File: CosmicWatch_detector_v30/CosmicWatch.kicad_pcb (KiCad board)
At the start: 2 copper layers, 140.8 x 104 mm, 111 parts, among them J3 RJ45, P1 CONN_01X04, P10 CONN_02X02, P11 CONN_01X01, P12 CONN_01X01, P13 CONN_01X01, P14 CONN_01X01, P15 CONN_02X04, P16 CONN_01X02, P19 CONN_01X01, P2 CONN_01X01, P29 CONN_01X01, P3 CONN_01X04, P30 CONN_01X01, P32 CONN_01X04, P4 CONN_01X04, P5 CONN_01X02, P7 CONN_01X01, P8 CONN_01X01, SW1 RESET, U1 LT3461, U10 SiPM_AFBR-S4N33C013, U12 LTC6752, U13 TS5A1066, U16 UMCC, U17 UMCC, U19 LMH6658, U2 SiPM_MicroFJ−300XX−TSV, U22 UMCC, U23 UMCC, U3 MMCX, U4 TS5A1066, U5 RasberryPi_Pico, U6 LMH6658, U7 TPS6040X, U8 sd_card_socket, U9 2NPNMBT6429DW1T1G

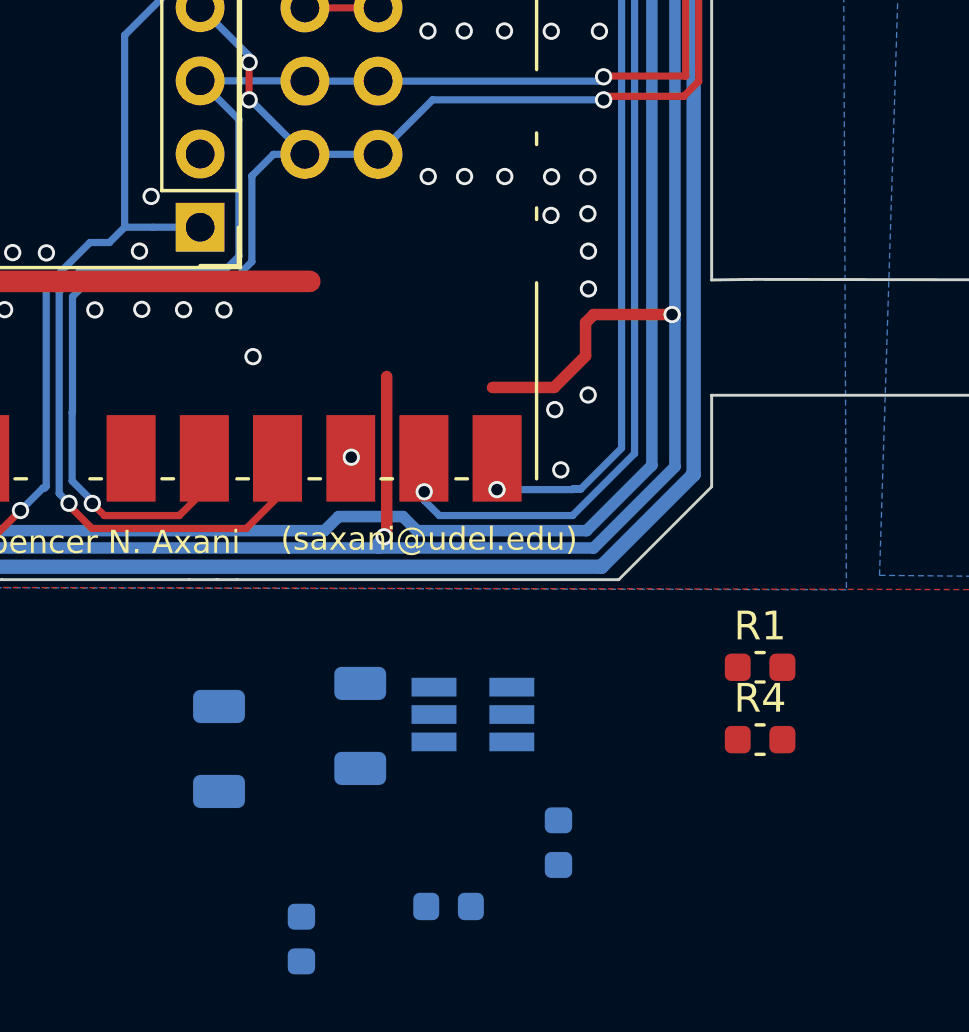
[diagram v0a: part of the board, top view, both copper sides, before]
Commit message: adding DC-DC booster on v3 schematics and pcb
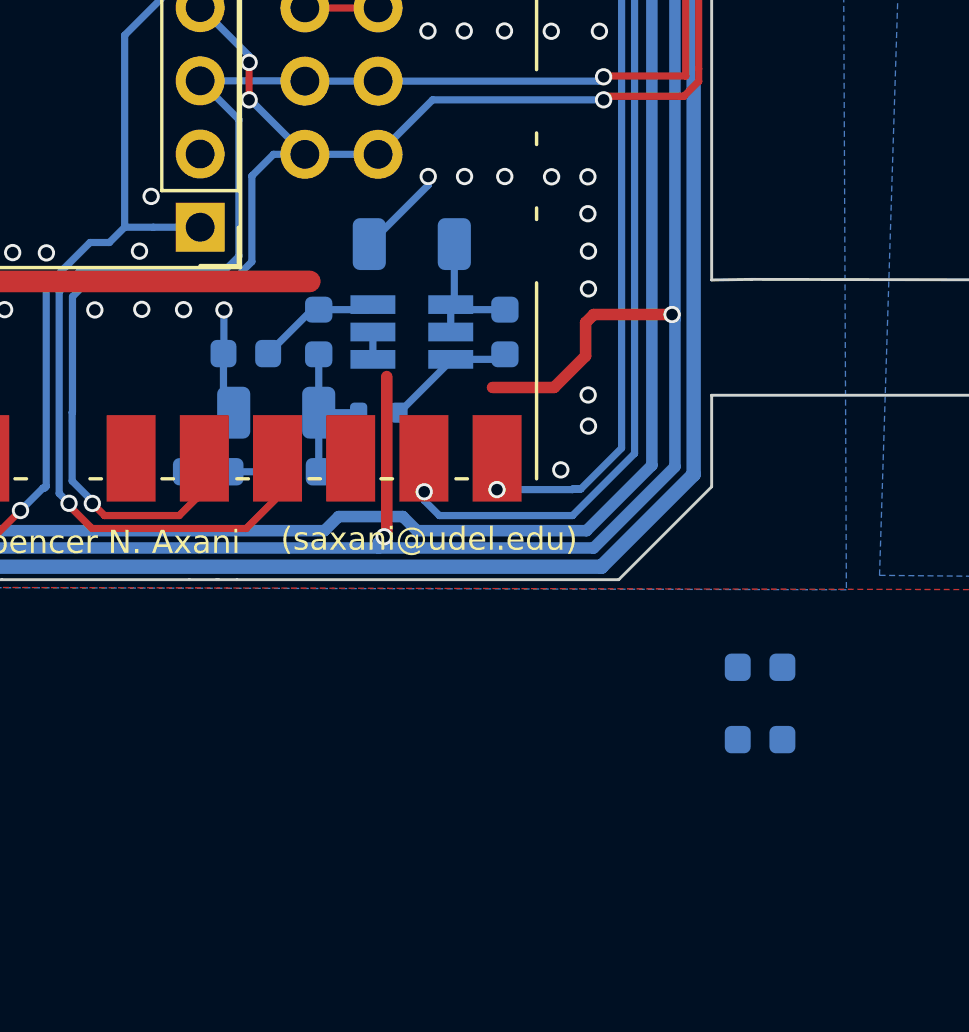
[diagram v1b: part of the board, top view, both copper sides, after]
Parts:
- removed C27: 2.2u, Capacitor_SMD:C_0603_1608Metric
- added C4: 1uF, Capacitor_SMD:C_0603_1608Metric, B.Cu at (179.8, 126.0)
- added D4: D_Schottky, Diode_SMD:D_SOD-523, B.Cu at (185.7, 123.9)
- added R10: 6.65k, Capacitor_SMD:C_0603_1608Metric, B.Cu at (181.1, 121.9)
- added R25: 100, Capacitor_SMD:C_0603_1608Metric, B.Cu at (182.8, 126.0)
- C2: value 4.7u -> 2.2uF
- C3: value 2.2u -> 2.2uF
- R1, R4: moved to B.Cu
- R2: value 1k -> 147k
- R24: value 10k -> 100k
- R40: value 100 -> 100k
- U1: value LT3461 -> MAX5026
- moved R2 21.1 mm to (183.6, 121.1), turned to -90 degrees
- moved L1 17.8 mm to (190.1, 121.1)
- moved C2 16.8 mm to (186.8, 118.1), turned to 180 degrees
- moved U1 13.4 mm to (186.8, 121.1), turned to 0 degrees
- moved C3 11.8 mm to (182.1, 123.9), turned to 180 degrees
- turned R1 to 180 degrees
- turned R4 to 180 degrees
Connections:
- C3 pad 1: HV -> Net-(D4-K)
- L1 pad 1: VCC -> Net-(D4-A)
- L1 pad 2: unconnected-(L1-Pad2) -> VCC
- R2 pad 1: unconnected-(R2-Pad1) -> Net-(U1-FB)
- R2 pad 2: HV -> Net-(D4-K)
- U1 pad 1: unconnected-(U1-sw-Pad1) -> GNDA
- U1 pad 2: unconnected-(U1-gnd-Pad2) -> GNDA
- U1 pad 3: unconnected-(U1-FB-Pad3) -> Net-(U1-FB)
- U1 pad 4: unconnected-(U1-SDWN-Pad4) -> VCC
- U1 pad 5: unconnected-(U1-Vout-Pad5) -> VCC
- U1 pad 6: VCC -> Net-(D4-A)
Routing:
- net GNDA: track 30.1 -> 40.7 mm, vias 319 -> 316
- net VCC: track 219.7 -> 226.3 mm
- net Net-(D4-K): track 0.00 -> 5.46 mm
- net Net-(D4-A): track 0.00 -> 4.55 mm
- net Net-(U1-FB): track 0.00 -> 4.34 mm

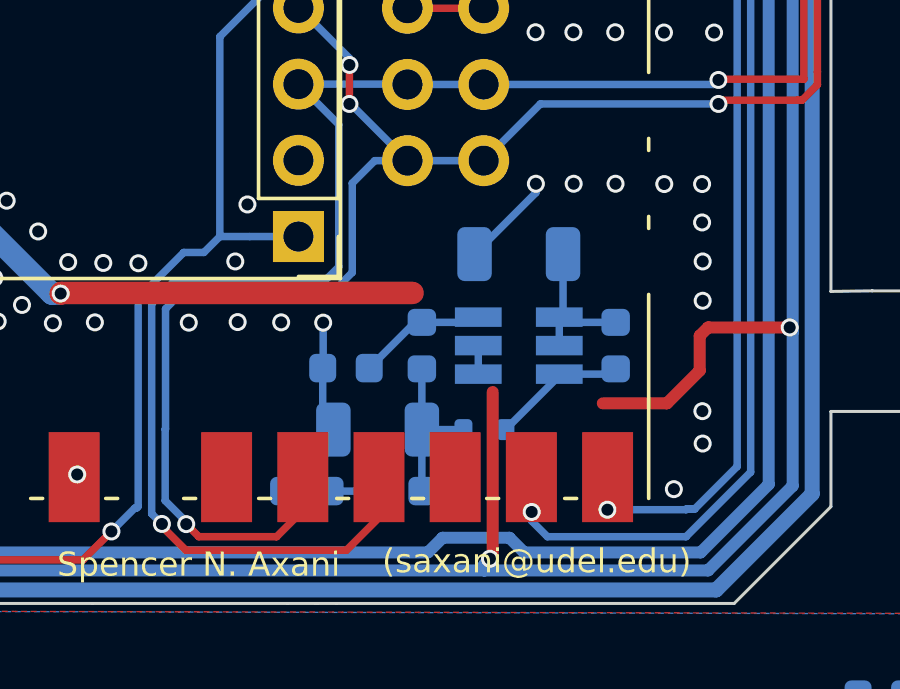
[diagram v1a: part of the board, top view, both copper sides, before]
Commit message: fixing misplaced VCC conection
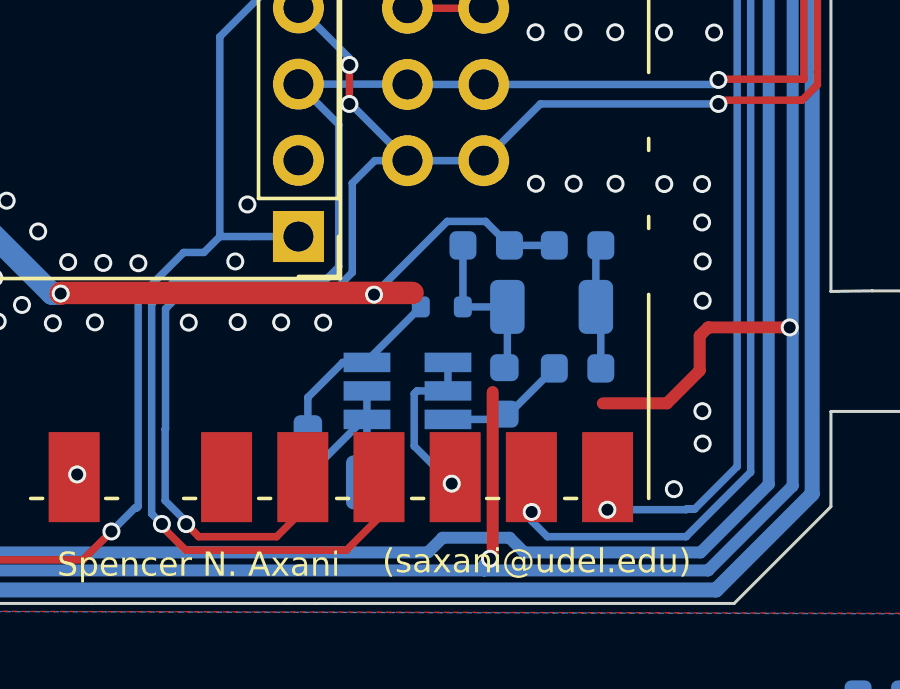
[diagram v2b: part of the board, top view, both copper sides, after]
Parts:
- moved C4 12.2 mm to (188.8, 117.8), turned to 0 degrees
- moved L1 10.9 mm to (179.8, 124.7), turned to -90 degrees
- moved R25 8.69 mm to (185.8, 117.8), turned to 180 degrees
- moved C2 8.47 mm to (183.1, 125.7), turned to 0 degrees
- moved R10 7.72 mm to (188.8, 121.9), turned to 180 degrees
- moved C3 7.10 mm to (187.9, 119.8), turned to 0 degrees
- moved D4 4.33 mm to (184.3, 119.8), turned to 180 degrees
- moved U1 4.01 mm to (183.1, 122.6), turned to 180 degrees
- moved R2 3.14 mm to (186.4, 122.6), turned to 90 degrees
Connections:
- C4 pad 1: VCC -> HV
- R25 pad 1: VCC -> HV
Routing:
- net HV: track 34.2 -> 41.5 mm, vias 3 -> 4
- net Net-(D4-A): track 4.55 -> 6.09 mm
- net GNDA: track 40.7 -> 40.0 mm, vias 316 -> 317
- net VCC: track 226.3 -> 225.6 mm

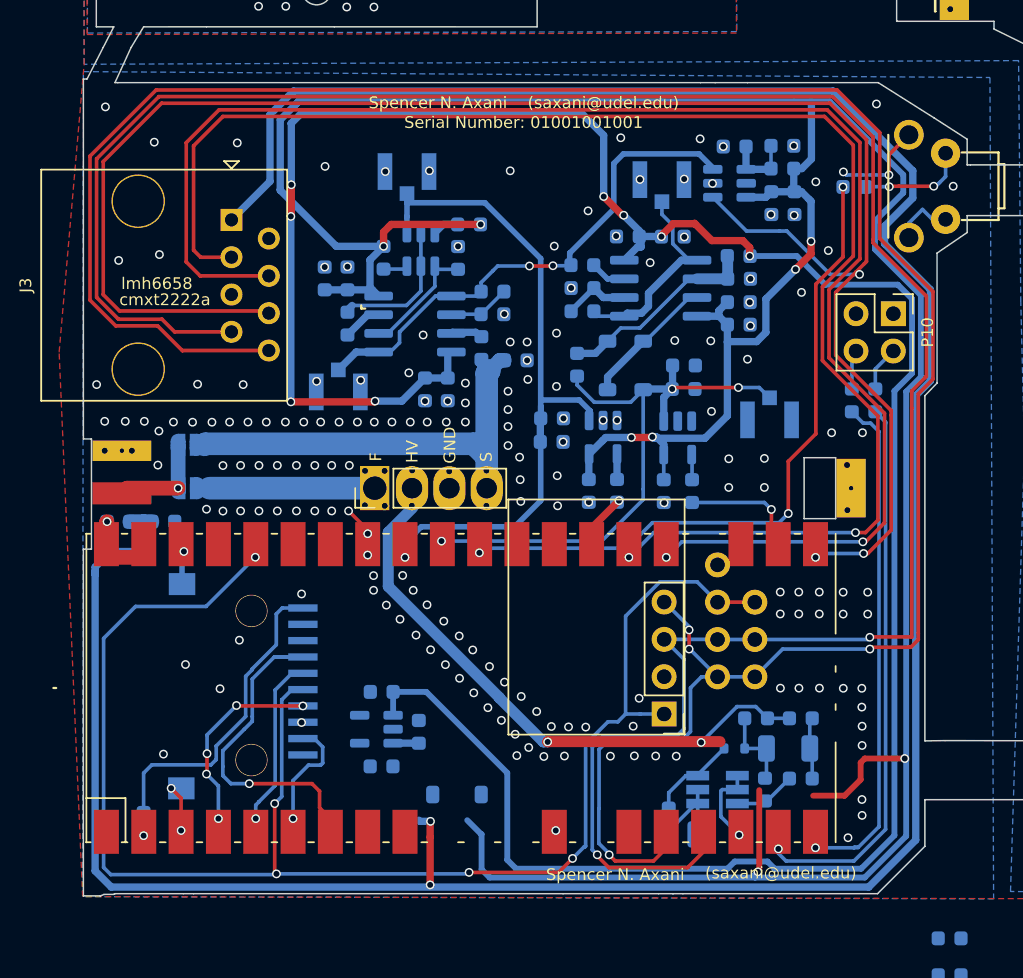
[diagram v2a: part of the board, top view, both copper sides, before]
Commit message: rearranging DC-DC booster components
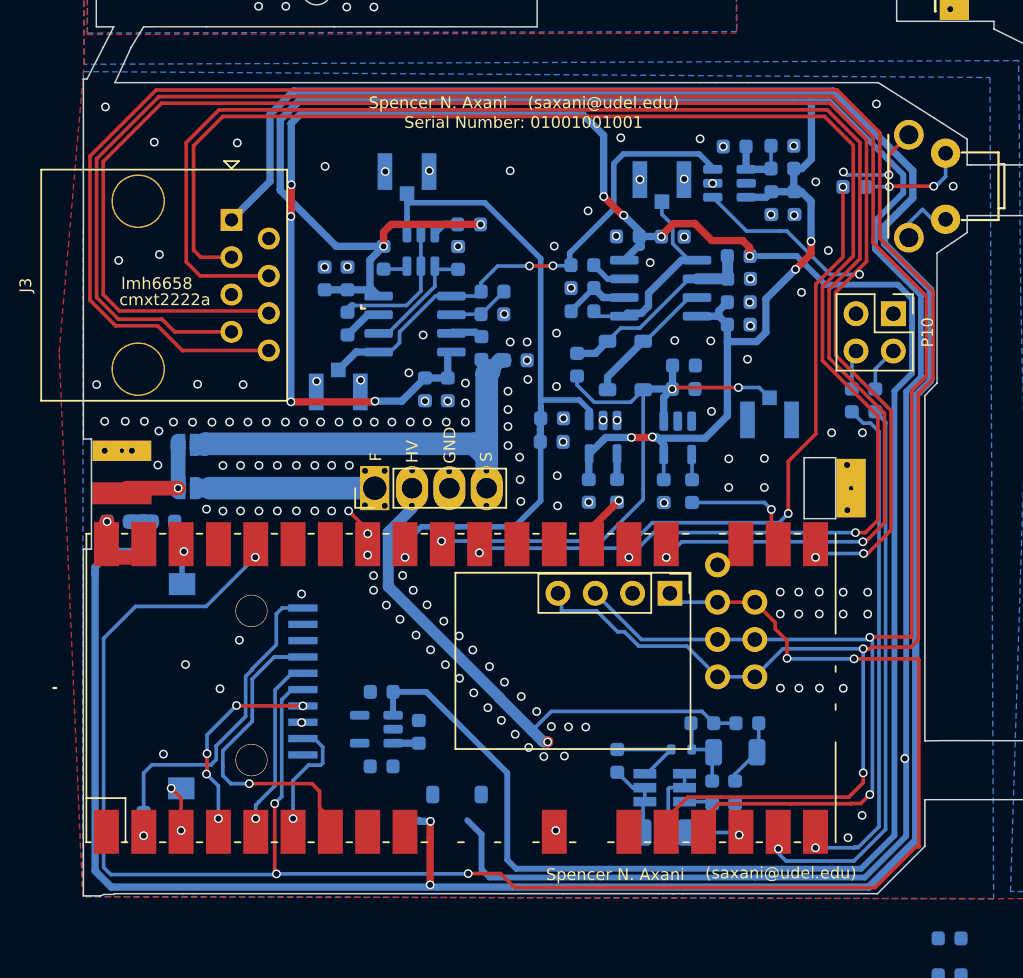
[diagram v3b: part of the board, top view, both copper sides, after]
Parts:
- moved P4 8.22 mm to (179.9, 109.3), turned to -90 degrees
- moved L1 5.31 mm to (176.3, 120.7)
- moved R10 4.57 mm to (184.3, 122.8), turned to -90 degrees
- moved R25 3.67 mm to (182.1, 118.1)
- moved C4 3.66 mm to (185.2, 118.1)
- moved C3 3.60 mm to (184.3, 120.1)
- moved D4 3.60 mm to (180.7, 119.9)
- moved R2 3.60 mm to (182.8, 122.8)
- moved C2 3.60 mm to (179.5, 125.5)
- moved U1 3.60 mm to (179.5, 122.5)
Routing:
- net 3.3V: track 106.0 -> 131.8 mm, vias 5 -> 7
- net VCC: track 225.6 -> 211.1 mm, vias 8 -> 7
- net SDA: track 161.7 -> 168.7 mm, vias 4 -> 2
- net HV: track 41.5 -> 37.2 mm, vias 4 -> 3
- net GNDA: track 40.0 -> 43.9 mm, vias 317 -> 305
- net Net-(U1-FB): track 4.25 -> 3.50 mm

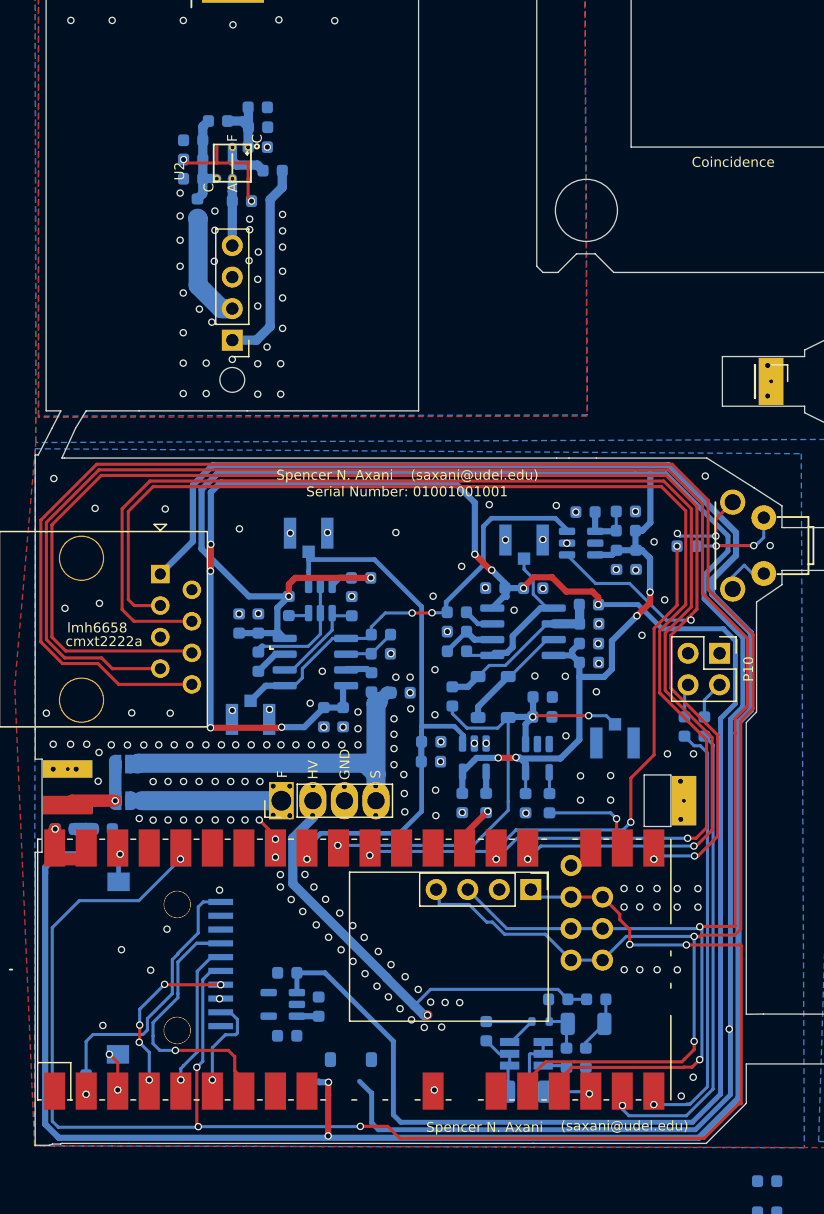
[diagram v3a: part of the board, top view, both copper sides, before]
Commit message: new booster added
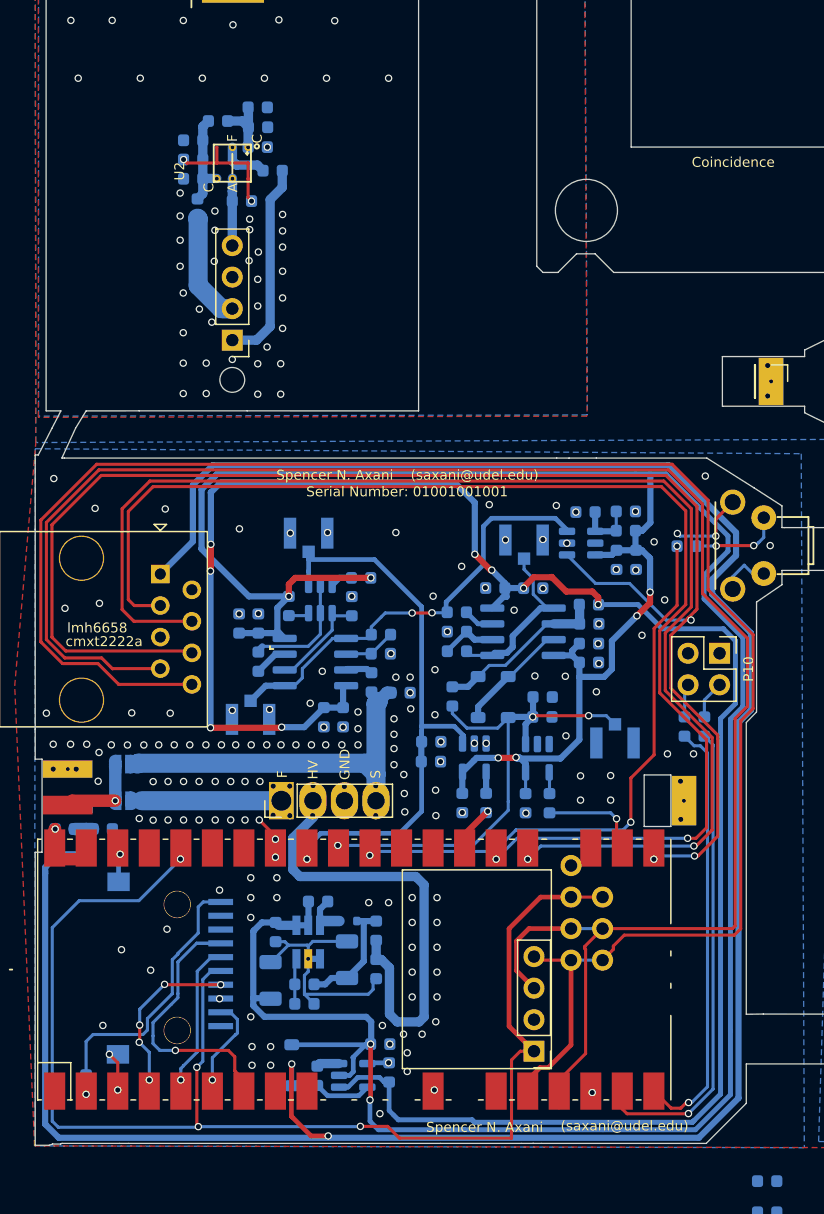
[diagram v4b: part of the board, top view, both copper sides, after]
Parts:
- added C7: 10nF, Capacitor_SMD:C_0603_1608Metric, B.Cu at (159.3, 112.7)
- C2: value 2.2uF -> 4.7uF
- moved R10 23.1 mm to (161.7, 118.5), turned to 180 degrees
- moved C2 22.5 mm to (158.9, 116.6), turned to 90 degrees
- moved R2 21.9 mm to (161.7, 116.9), turned to 0 degrees
- moved C3 19.9 mm to (165.1, 114.9), turned to 90 degrees
- moved U1 19.7 mm to (162.0, 113.5), turned to 90 degrees
- moved C4 17.9 mm to (167.4, 115.7), turned to -90 degrees
- moved D4 17.5 mm to (165.2, 111.8)
- moved L1 17.1 mm to (162.8, 110.2), turned to 180 degrees
- moved R25 15.7 mm to (167.4, 112.6), turned to 90 degrees
- moved P4 13.0 mm to (180.2, 122.3), turned to 180 degrees
- moved C42 11.5 mm to (168.5, 124.0), turned to 90 degrees
- moved U7 8.05 mm to (165.6, 124.2), turned to 0 degrees
- moved C47 7.52 mm to (167.8, 121.7), turned to 180 degrees
- moved C41 5.57 mm to (162.7, 124.3), turned to 90 degrees
- moved D1 4.78 mm to (160.6, 123.4), turned to -90 degrees
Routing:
- net VCC: track 211.1 -> 244.4 mm, vias 7 -> 8
- net 3.3V: track 131.8 -> 107.4 mm, vias 7 -> 4
- net SDA: track 168.7 -> 146.1 mm, vias 2 -> 0
- net GNDA: track 43.9 -> 55.5 mm, vias 305 -> 298
- net VEE: track 167.9 -> 157.8 mm
- net SCL: track 159.3 -> 149.7 mm, vias 2 -> 0
- net Net-(U7-Cfly+): track 0.00 -> 4.66 mm
- net VBUS: track 193.8 -> 198.3 mm
- net Net-(D4-K): track 5.38 -> 9.57 mm
- net Net-(D4-A): track 6.14 -> 3.88 mm
- net Net-(U5-GP15): track 36.5 -> 38.4 mm
- net Net-(U5-GP14): track 39.5 -> 41.4 mm
- net Net-(D2-K): track 9.84 -> 8.66 mm
- net Net-(D2-A): track 13.9 -> 13.3 mm
- net HV: track 37.2 -> 37.6 mm, vias 3 -> 2
